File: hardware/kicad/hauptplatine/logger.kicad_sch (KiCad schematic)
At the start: 0 parts

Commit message: Wetter-Eingang hinzugefügt
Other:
- added sheet MCU (mcu.kicad_sch)
- note added: "Blätter: Versorgung, MCU (fertig). Folgen: Funk + Flash, Waage, Mikrofon, Anschlüsse."
- note removed: "Blätter: Versorgung (fertig). Folgen: MCU, Funk + Flash, Waage, Mikrofon, Anschlüsse."
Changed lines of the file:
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@@
 		(comment 3 "Umgebung [A]: Gehäuse −20 … +60 °C, Betauung möglich; VIN ≤ 12 V dauernd, 25 V absolut")
 	)
-	(text "Blätter: Versorgung (fertig). Folgen: MCU, Funk + Flash, Waage, Mikrofon, Anschlüsse."
+	(text "Blätter: Versorgung, MCU (fertig). Folgen: Funk + Flash, Waage, Mikrofon, Anschlüsse."
 		(exclude_from_sim no)
 		(at 30 25 0)
@@
 		)
 	)
+	(sheet
+		(at 85 40)
+		(size 45 20)
+		(exclude_from_sim no)
+		(in_bom yes)
+		(on_board yes)
+		(dnp no)
+		(fields_autoplaced yes)
+		(stroke
+			(width 0.1524)
+			(type solid)
+		)
+		(fill
+			(color 0 0 0 0)
+		)
+		(property "Sheetname" "MCU"
+			(at 85 39.3 0)
+			(show_name no)
+			(do_not_autoplace no)
+			(effects
+				(font
+					(size 1.27 1.27)
+				)
+				(justify left bottom)
+			)
+		)
+		(property "Sheetfile" "mcu.kicad_sch"
+			(at 85 60.6 0)
+			(show_name no)
+			(do_not_autoplace no)
+			(effects
+				(font
+					(size 1.27 1.27)
+				)
+				(justify left top)
+			)
+		)
+		(instances
+			(project "logger"
+				(path "/69595bfe-3184-5a98-8dcb-39e42f38dc44"
+					(page "3")
+				)
+			)
+		)
+	)

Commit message: Hardware update
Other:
- added sheet Funk + Flash (funk.kicad_sch)
- note added: "Blätter: Versorgung, MCU, Funk + Flash (fertig). Folgen: Waage, Mikrofon, Anschlüsse."
- note removed: "Blätter: Versorgung, MCU (fertig). Folgen: Funk + Flash, Waage, Mikrofon, Anschlüsse."
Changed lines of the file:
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@@
 		(comment 3 "Umgebung [A]: Gehäuse −20 … +60 °C, Betauung möglich; VIN ≤ 12 V dauernd, 25 V absolut")
 	)
-	(text "Blätter: Versorgung, MCU (fertig). Folgen: Funk + Flash, Waage, Mikrofon, Anschlüsse."
+	(text "Blätter: Versorgung, MCU, Funk + Flash (fertig). Folgen: Waage, Mikrofon, Anschlüsse."
 		(exclude_from_sim no)
 		(at 30 25 0)
@@
 		)
 	)
+	(sheet
+		(at 140 40)
+		(size 45 20)
+		(exclude_from_sim no)
+		(in_bom yes)
+		(on_board yes)
+		(dnp no)
+		(fields_autoplaced yes)
+		(stroke
+			(width 0.1524)
+			(type solid)
+		)
+		(fill
+			(color 0 0 0 0)
+		)
+		(property "Sheetname" "Funk + Flash"
+			(at 140 39.3 0)
+			(show_name no)
+			(do_not_autoplace no)
+			(effects
+				(font
+					(size 1.27 1.27)
+				)
+				(justify left bottom)
+			)
+		)
+		(property "Sheetfile" "funk.kicad_sch"
+			(at 140 60.6 0)
+			(show_name no)
+			(do_not_autoplace no)
+			(effects
+				(font
+					(size 1.27 1.27)
+				)
+				(justify left top)
+			)
+		)
+		(instances
+			(project "logger"
+				(path "/69595bfe-3184-5a98-8dcb-39e42f38dc44"
+					(page "4")
+				)
+			)
+		)
+	)

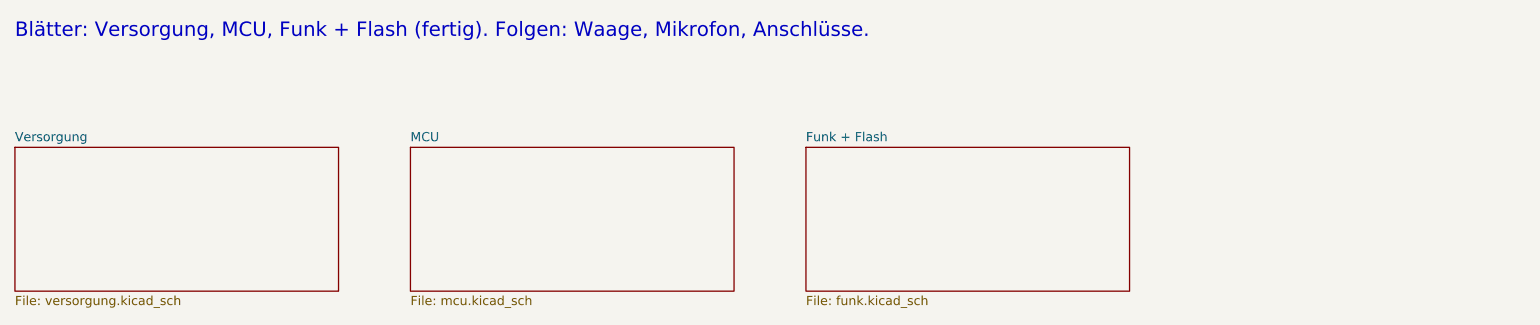
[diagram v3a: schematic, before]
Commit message: update
chaltplanblatt Waage (SCH26-07): TPS61240, HX711, J501=J4; netz_tests 114
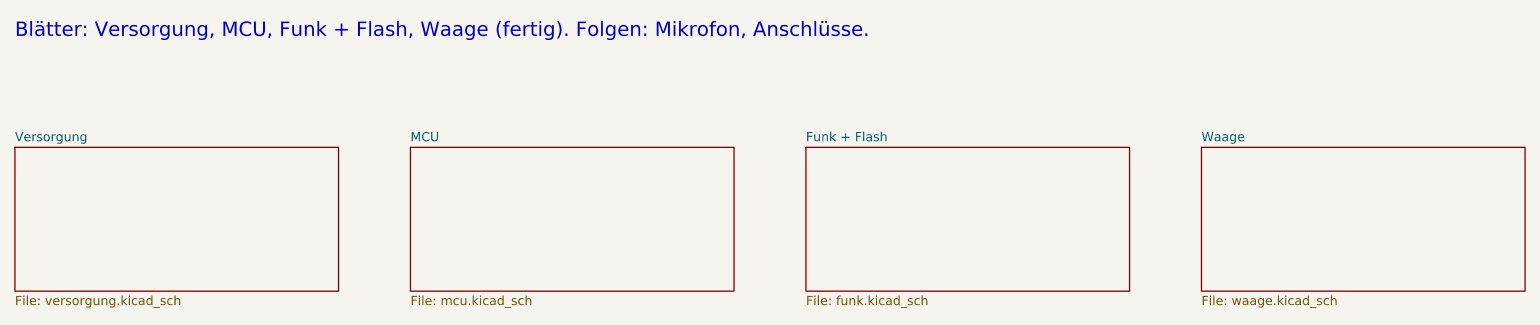
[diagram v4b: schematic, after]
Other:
- added sheet Waage (waage.kicad_sch)
- note added: "Blätter: Versorgung, MCU, Funk + Flash, Waage (fertig). Folgen: Mikrofon, Anschlüsse."
- note removed: "Blätter: Versorgung, MCU, Funk + Flash (fertig). Folgen: Waage, Mikrofon, Anschlüsse."
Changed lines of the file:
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@@
 		(comment 3 "Umgebung [A]: Gehäuse −20 … +60 °C, Betauung möglich; VIN ≤ 12 V dauernd, 25 V absolut")
 	)
-	(text "Blätter: Versorgung, MCU, Funk + Flash (fertig). Folgen: Waage, Mikrofon, Anschlüsse."
+	(text "Blätter: Versorgung, MCU, Funk + Flash, Waage (fertig). Folgen: Mikrofon, Anschlüsse."
 		(exclude_from_sim no)
 		(at 30 25 0)
@@
 				)
 			)
+		)
+	)
+	(sheet
+		(at 195 40)
+		(size 45 20)
+		(exclude_from_sim no)
+		(in_bom yes)
+		(on_board yes)
+		(dnp no)
+		(fields_autoplaced yes)
+		(stroke
+			(width 0.1524)
+			(type solid)
+		)
+		(fill
+			(color 0 0 0 0)
+		)
+		(property "Sheetname" "Waage"
+			(at 195 39.3 0)
+			(show_name no)
+			(do_not_autoplace no)
+			(effects
+				(font
+					(size 1.27 1.27)
+				)
+				(justify left bottom)
+			)
+		)
+		(property "Sheetfile" "waage.kicad_sch"
+			(at 195 60.6 0)
+			(show_name no)
+			(do_not_autoplace no)
+			(effects
+				(font
+					(size 1.27 1.27)
+				)
+				(justify left top)
+			)
+		)
+		(instances
+			(project "logger"
+				(path "/69595bfe-3184-5a98-8dcb-39e42f38dc44"
+					(page "5")
+				)
+			)

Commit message: update
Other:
- added sheet Mikrofon (mikrofon.kicad_sch)
- note added: "Blätter: Versorgung, MCU, Funk + Flash, Waage, Mikrofon (fertig). Folgt: Anschlüsse."
- note removed: "Blätter: Versorgung, MCU, Funk + Flash, Waage (fertig). Folgen: Mikrofon, Anschlüsse."
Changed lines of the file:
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@@
 		(comment 3 "Umgebung [A]: Gehäuse −20 … +60 °C, Betauung möglich; VIN ≤ 12 V dauernd, 25 V absolut")
 	)
-	(text "Blätter: Versorgung, MCU, Funk + Flash, Waage (fertig). Folgen: Mikrofon, Anschlüsse."
+	(text "Blätter: Versorgung, MCU, Funk + Flash, Waage, Mikrofon (fertig). Folgt: Anschlüsse."
 		(exclude_from_sim no)
 		(at 30 25 0)
@@
 				)
 			)
+		)
+	)
+	(sheet
+		(at 250 40)
+		(size 45 20)
+		(exclude_from_sim no)
+		(in_bom yes)
+		(on_board yes)
+		(dnp no)
+		(fields_autoplaced yes)
+		(stroke
+			(width 0.1524)
+			(type solid)
+		)
+		(fill
+			(color 0 0 0 0)
+		)
+		(property "Sheetname" "Mikrofon"
+			(at 250 39.3 0)
+			(show_name no)
+			(do_not_autoplace no)
+			(effects
+				(font
+					(size 1.27 1.27)
+				)
+				(justify left bottom)
+			)
+		)
+		(property "Sheetfile" "mikrofon.kicad_sch"
+			(at 250 60.6 0)
+			(show_name no)
+			(do_not_autoplace no)
+			(effects
+				(font
+					(size 1.27 1.27)
+				)
+				(justify left top)
+			)
+		)
+		(instances
+			(project "logger"
+				(path "/69595bfe-3184-5a98-8dcb-39e42f38dc44"
+					(page "6")
+				)
+			)

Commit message: update
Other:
- added sheet Anschlüsse (anschluesse.kicad_sch)
- note added: "Blätter: Versorgung, MCU, Funk + Flash, Waage, Mikrofon, Anschlüsse (Entwurf vollständig)."
- note removed: "Blätter: Versorgung, MCU, Funk + Flash, Waage, Mikrofon (fertig). Folgt: Anschlüsse."
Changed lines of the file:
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@@
 		(comment 3 "Umgebung [A]: Gehäuse −20 … +60 °C, Betauung möglich; VIN ≤ 12 V dauernd, 25 V absolut")
 	)
-	(text "Blätter: Versorgung, MCU, Funk + Flash, Waage, Mikrofon (fertig). Folgt: Anschlüsse."
+	(text "Blätter: Versorgung, MCU, Funk + Flash, Waage, Mikrofon, Anschlüsse (Entwurf vollständig)."
 		(exclude_from_sim no)
 		(at 30 25 0)
@@
 				)
 			)
+		)
+	)
+	(sheet
+		(at 305 40)
+		(size 45 20)
+		(exclude_from_sim no)
+		(in_bom yes)
+		(on_board yes)
+		(dnp no)
+		(fields_autoplaced yes)
+		(stroke
+			(width 0.1524)
+			(type solid)
+		)
+		(fill
+			(color 0 0 0 0)
+		)
+		(property "Sheetname" "Anschlüsse"
+			(at 305 39.3 0)
+			(show_name no)
+			(do_not_autoplace no)
+			(effects
+				(font
+					(size 1.27 1.27)
+				)
+				(justify left bottom)
+			)
+		)
+		(property "Sheetfile" "anschluesse.kicad_sch"
+			(at 305 60.6 0)
+			(show_name no)
+			(do_not_autoplace no)
+			(effects
+				(font
+					(size 1.27 1.27)
+				)
+				(justify left top)
+			)
+		)
+		(instances
+			(project "logger"
+				(path "/69595bfe-3184-5a98-8dcb-39e42f38dc44"
+					(page "7")
+				)
+			)

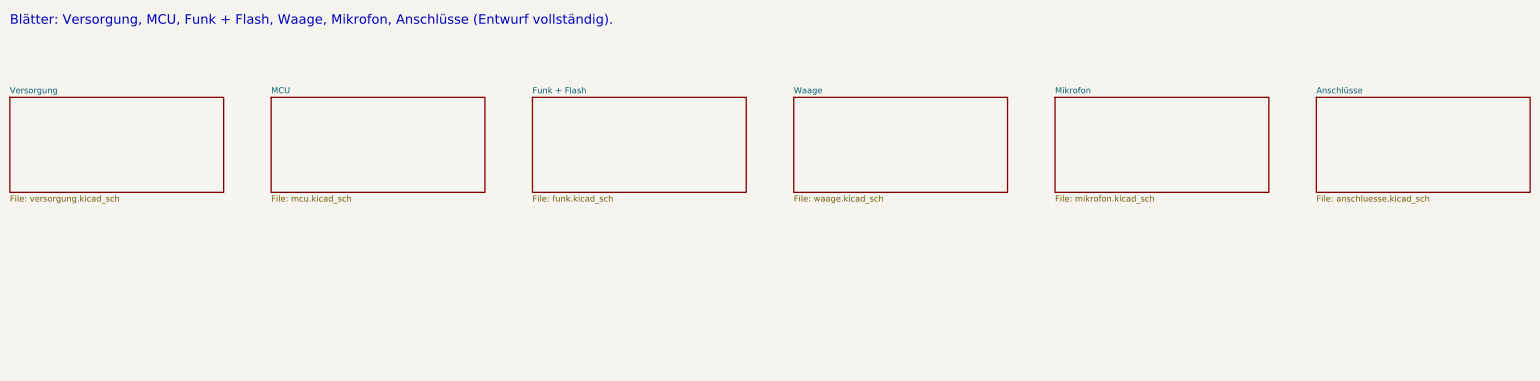
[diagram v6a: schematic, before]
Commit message: HW-06: Akku auf der Hauptplatine (Blatt Akku, Akku-Platine entfällt); HW-05: USB mit VBUS-Erkennung an PB13; Routing-Werkzeuge; Aufräumen: Restbezüge Akku-Platine, README-Stand; ERC 0, Netzprüfung 168/168, Pin/Footprint 0; Platine platziert, nicht geroutet
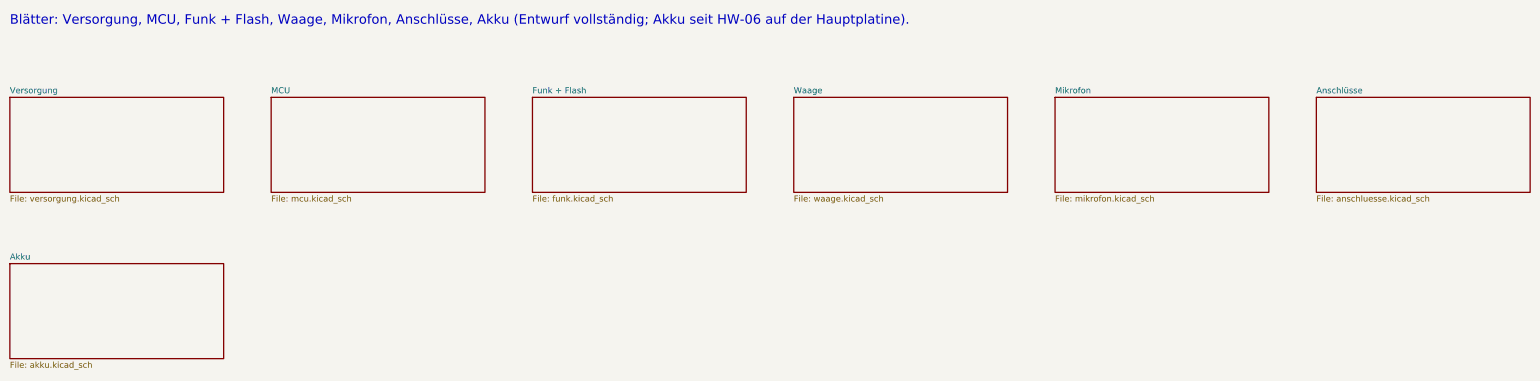
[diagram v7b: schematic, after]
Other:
- added sheet Akku (akku.kicad_sch)
- note added: "Blätter: Versorgung, MCU, Funk + Flash, Waage, Mikrofon, Anschlüsse, Akku (Entwurf vollständig; Akku seit HW-06 auf der Hauptplatine)."
- note removed: "Blätter: Versorgung, MCU, Funk + Flash, Waage, Mikrofon, Anschlüsse (Entwurf vollständig)."
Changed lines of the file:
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@@
 		(comment 3 "Umgebung [A]: Gehäuse −20 … +60 °C, Betauung möglich; VIN ≤ 12 V dauernd, 25 V absolut")
 	)
-	(text "Blätter: Versorgung, MCU, Funk + Flash, Waage, Mikrofon, Anschlüsse (Entwurf vollständig)."
+	(text "Blätter: Versorgung, MCU, Funk + Flash, Waage, Mikrofon, Anschlüsse, Akku (Entwurf vollständig; Akku seit HW-06 auf der Hauptplatine)."
 		(exclude_from_sim no)
 		(at 30 25 0)
@@
 		)
 	)
+	(sheet
+		(at 30 75)
+		(size 45 20)
+		(exclude_from_sim no)
+		(in_bom yes)
+		(on_board yes)
+		(dnp no)
+		(fields_autoplaced yes)
+		(stroke
+			(width 0.1524)
+			(type solid)
+		)
+		(fill
+			(color 0 0 0 0)
+		)
+		(property "Sheetname" "Akku"
+			(at 30 74.3 0)
+			(show_name no)
+			(do_not_autoplace no)
+			(effects
+				(font
+					(size 1.27 1.27)
+				)
+				(justify left bottom)
+			)
+		)
+		(property "Sheetfile" "akku.kicad_sch"
+			(at 30 95.6 0)
+			(show_name no)
+			(do_not_autoplace no)
+			(effects
+				(font
+					(size 1.27 1.27)
+				)
+				(justify left top)
+			)
+		)
+		(instances
+			(project "logger"
+				(path "/69595bfe-3184-5a98-8dcb-39e42f38dc44"
+					(page "8")
+				)
+			)
+		)
+	)
